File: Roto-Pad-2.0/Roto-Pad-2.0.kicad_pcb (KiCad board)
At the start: 2 copper layers, 103 x 127.5 mm, 115 parts, among them Q1 BSS138, SW1 Switch, SW10 Switch, SW11 Switch, SW12 Switch, SW13 Switch, SW14 Switch, SW15 Switch, SW16 Switch, SW17 Switch, SW18 Switch, SW19 Switch, SW2 Switch, SW20 Switch, SW21 Switch, SW22 Switch, SW23 Switch, SW24 Switch, SW25 Switch, SW3 Switch, SW4 Switch, SW5 Switch, SW6 Switch, SW7 Switch, SW8 Switch, SW9 Switch, U1 Pico

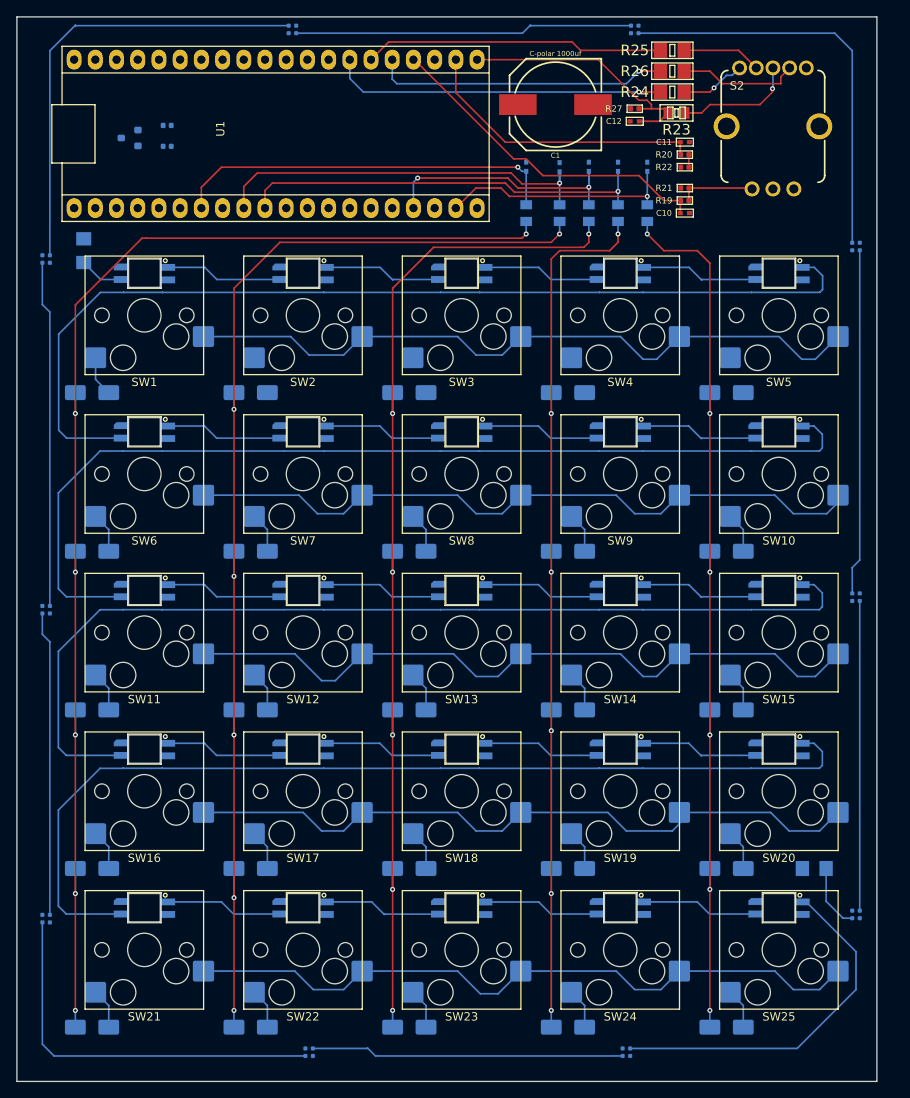
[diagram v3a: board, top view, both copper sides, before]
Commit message: finished initial routing
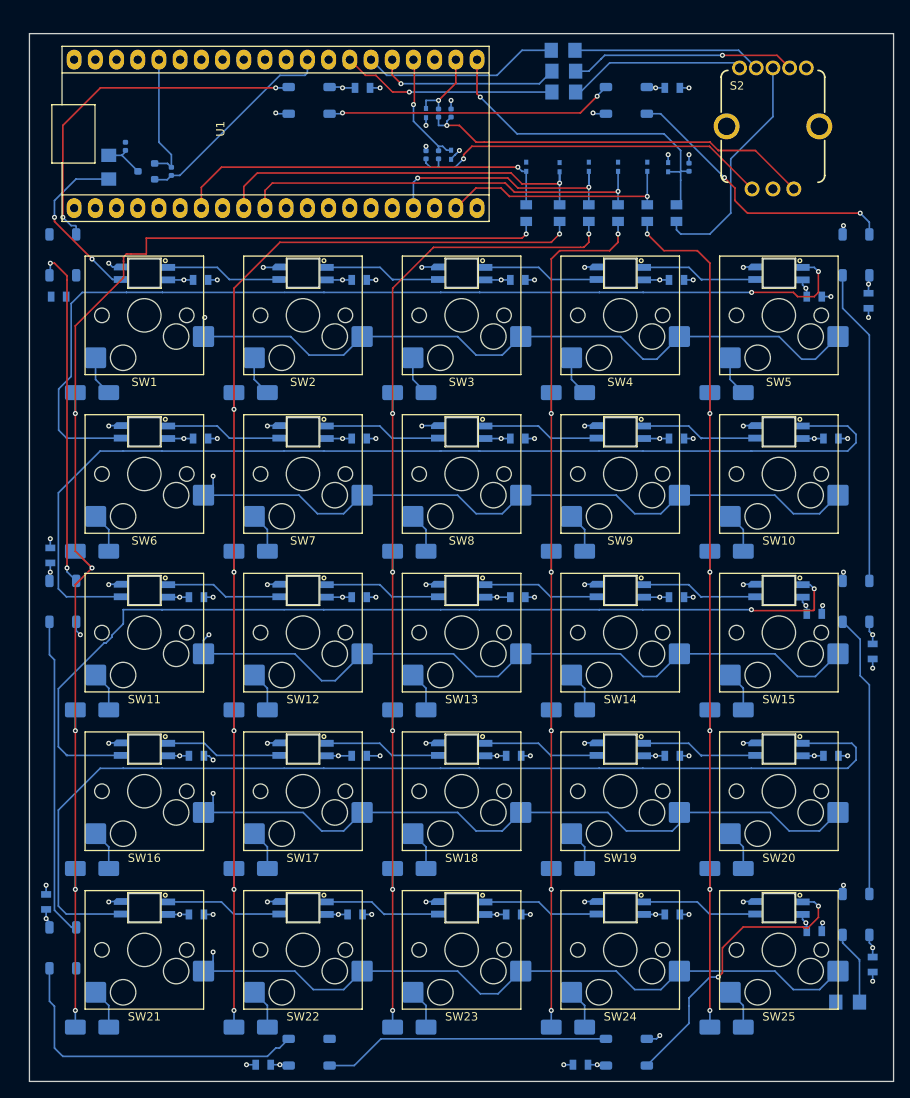
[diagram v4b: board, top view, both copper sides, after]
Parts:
- removed C1: C-polar 1000uf, Capacitors:NIC_10X10.5_CAP
- added C13: Capacitor, Capacitors:0805, B.Cu at (124.0, 55.5)
- added C14: Capacitor, Capacitors:0805, B.Cu at (140.5, 57.5)
- added C15: Capacitor, Capacitors:0805, B.Cu at (67.0, 74.5)
- added C16: Capacitor, Capacitors:0805, B.Cu at (86.0, 74.5)
- added C17: Capacitor, Capacitors:0805, B.Cu at (105.0, 74.5)
- added C18: Capacitor, Capacitors:0805, B.Cu at (124.0, 74.5)
- added C19: Capacitor, Capacitors:0805, B.Cu at (142.5, 74.5)
- added C2: 47uF, Capacitors:0805, B.Cu at (67.0, 55.5)
- added C20: Capacitor, Capacitors:0805, B.Cu at (66.5, 93.5)
- added C21: Capacitor, Capacitors:0805, B.Cu at (86.0, 93.5)
- added C22: Capacitor, Capacitors:0805, B.Cu at (105.0, 93.5)
- added C23: Capacitor, Capacitors:0805, B.Cu at (124.0, 93.5)
- added C24: Capacitor, Capacitors:0805, B.Cu at (140.5, 95.5)
- added C25: Capacitor, Capacitors:0805, B.Cu at (66.5, 112.5)
- added C26: Capacitor, Capacitors:0805, B.Cu at (86.0, 112.5)
- added C27: Capacitor, Capacitors:0805, B.Cu at (104.5, 112.5)
- added C28: Capacitor, Capacitors:0805, B.Cu at (123.5, 112.5)
- added C29: Capacitor, Capacitors:0805, B.Cu at (142.5, 112.5)
- added C3: Capacitor, Capacitors:0805, B.Cu at (86.0, 55.5)
- added C30: Capacitor, Capacitors:0805, B.Cu at (66.5, 131.5)
- added C31: Capacitor, Capacitors:0805, B.Cu at (85.5, 131.5)
- added C32: Capacitor, Capacitors:0805, B.Cu at (104.5, 131.5)
- added C33: Capacitor, Capacitors:0805, B.Cu at (123.5, 131.5)
- added C34: Capacitor, Capacitors:0805, B.Cu at (140.5, 133.5)
- added C35: Capacitor, Capacitors:0805, B.Cu at (112.5, 149.5)
- added C36: Capacitor, Capacitors:0805, B.Cu at (48.5, 130.0)
- added C37: Capacitor, Capacitors:0805, B.Cu at (49.0, 88.5)
- added C38: Capacitor, Capacitors:0805, B.Cu at (74.5, 149.5)
- added C39: Capacitor, Capacitors:0805, B.Cu at (50.0, 57.5)
- added C4: Capacitor, Capacitors:0805, B.Cu at (105.0, 55.5)
- added C40: Capacitor, Capacitors:0805, B.Cu at (86.4, 32.5)
- added C41: Capacitor, Capacitors:0805, B.Cu at (123.5, 32.5)
- added C42: Capacitor, Capacitors:0805, B.Cu at (147.0, 58.0)
- added C43: Capacitor, Capacitors:0805, B.Cu at (147.5, 100.0)
- added C44: Capacitor, Capacitors:0805, B.Cu at (147.5, 137.5)
- C10, C11, C12, R19, R20, R21, R22, R23, R24, R25, R26, R27: moved to B.Cu
- LED26, LED27, LED28, LED29, LED30, LED31, LED32, LED33, LED34, LED35: footprint PCM_LED_SMD_AKL:LED_SK6812_EC15_1.5x1.5mm -> PCM_LED_SMD_AKL:LED_SK6812_PLCC4_5.0x5.0mm_P3.2mm
- moved R21 31.3 mm to (94.0, 40.5), turned to 90 degrees
- moved C11 31.2 mm to (94.0, 35.5), turned to 90 degrees
- moved R19 30.0 mm to (95.5, 40.5), turned to -90 degrees
- moved R20 29.9 mm to (95.5, 35.5), turned to -90 degrees
- moved C10 28.9 mm to (97.0, 40.5), turned to 90 degrees
- moved R22 28.7 mm to (97.0, 35.5), turned to -90 degrees
- moved R9 16.5 mm to (144.5, 142.0)
- moved R25 13.1 mm to (110.4, 28.0)
- moved R24 13.0 mm to (110.5, 33.0)
- moved R26 13.0 mm to (110.5, 30.5)
- moved R23 12.0 mm to (124.0, 47.5), turned to -90 degrees
- moved R10 10.4 mm to (56.0, 42.0)
- moved R27 9.55 mm to (125.5, 42.0), turned to 90 degrees
- moved LED31 8.73 mm to (80.0, 34.0), turned to 0 degrees
- moved LED32 8.56 mm to (118.0, 34.0), turned to 0 degrees
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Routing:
- net /Key Matrix/Row 5: track 83.8 -> 180.6 mm, vias 0 -> 1
- net 5v: track 0.00 -> 91.6 mm, vias 0 -> 36
- net GND: track 0.00 -> 91.0 mm, vias 0 -> 70
- net /Key Matrix/Row 4: track 84.1 -> 160.9 mm, vias 0 -> 1
- net /Key Matrix/Row 3: track 85.4 -> 144.3 mm, vias 0 -> 1
- net /Key Matrix/Row 2: track 83.8 -> 131.3 mm, vias 0 -> 1
- net Net-(R20--): track 1.59 -> 47.9 mm, vias 0 -> 1
- net Net-(R19--): track 9.11 -> 44.4 mm, vias 0 -> 1
- net /Key Matrix/Row 1: track 84.2 -> 111.1 mm, vias 0 -> 1
- net /RGB Encoder/enc A: track 40.5 -> 14.1 mm, vias 0 -> 1
- net /RGB Encoder/enc B: track 34.8 -> 9.23 mm, vias 0 -> 1
- net /Neopixel Logic Shifter/sigLOW: track 0.00 -> 25.2 mm
- net /Neopixel Logic Shifter/3.3v: track 0.00 -> 15.7 mm
- net Net-(LED1-DIN): track 5.29 -> 20.9 mm, vias 0 -> 2
- net Net-(LED32-DOUT): track 49.5 -> 34.4 mm, vias 0 -> 2
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- added copper zone on In2.Cu, net 5v
- added copper zone on In1.Cu, net GND
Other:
- board size 103 x 127.5 mm -> 103.5 x 125.5 mm
- copper layers 2 -> 4

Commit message: PCB passes DRC
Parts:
- R14, R15, R16, R17, R18, R23: footprint adafruit:R0805 -> Custom:R0805
- moved C39 13.5 mm to (49.0, 44.0), turned to 90 degrees
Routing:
- net GND: track 91.0 -> 101.3 mm, vias 70 -> 79
- net 5v: track 91.6 -> 97.9 mm, vias 36 -> 38
- net /Key Matrix/Row 2: track 131.3 -> 128.9 mm
